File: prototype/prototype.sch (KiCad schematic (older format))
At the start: 31 parts, among them P1 CONN_25X2, P2 CONN_25X2, P3 VGACONN, U1 MC68SEC000

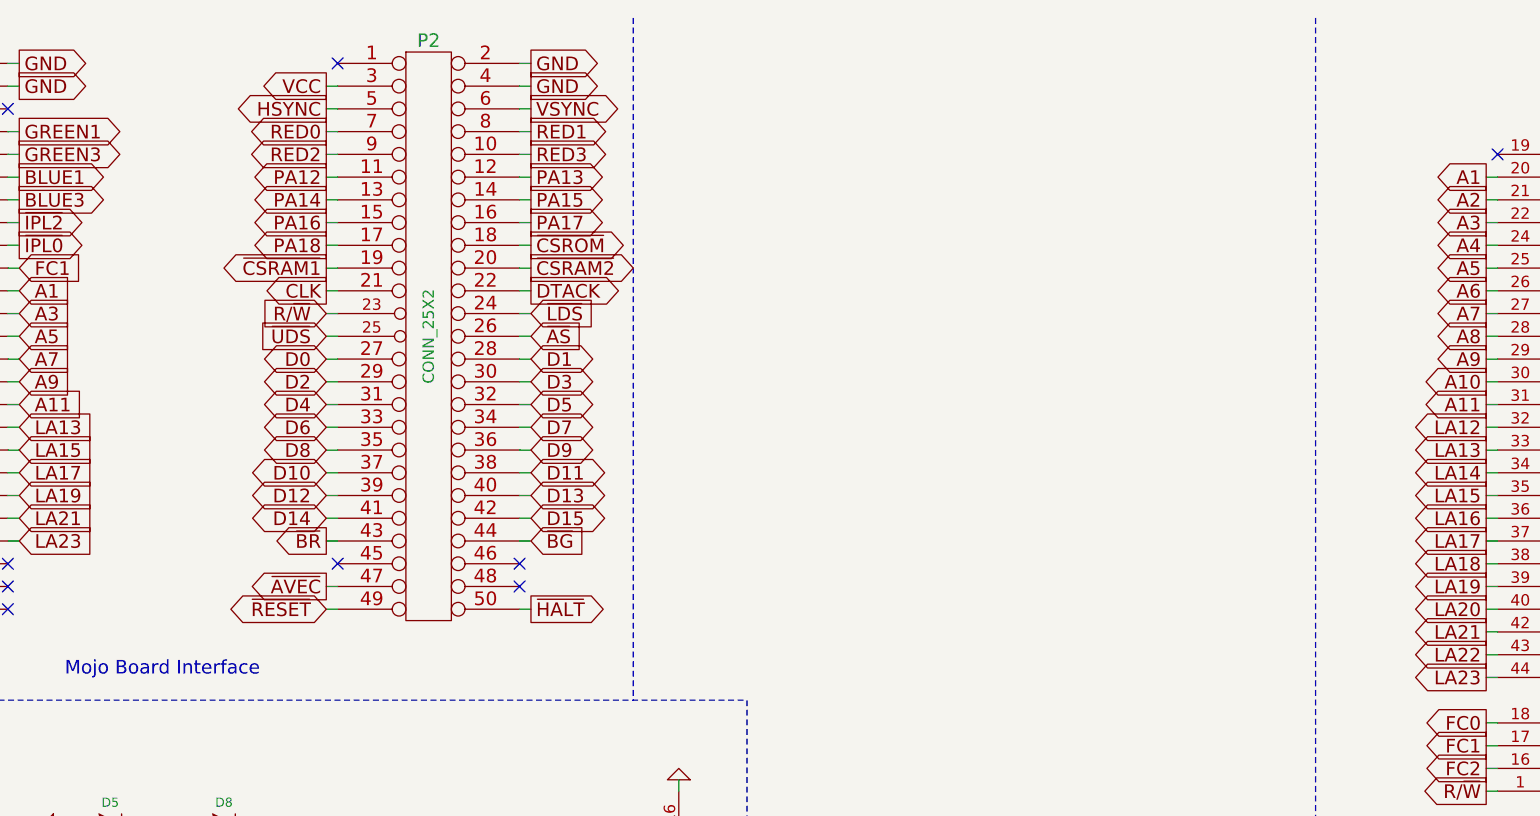
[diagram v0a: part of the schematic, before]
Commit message: Add the flash ROM chip to the prototype schematic.
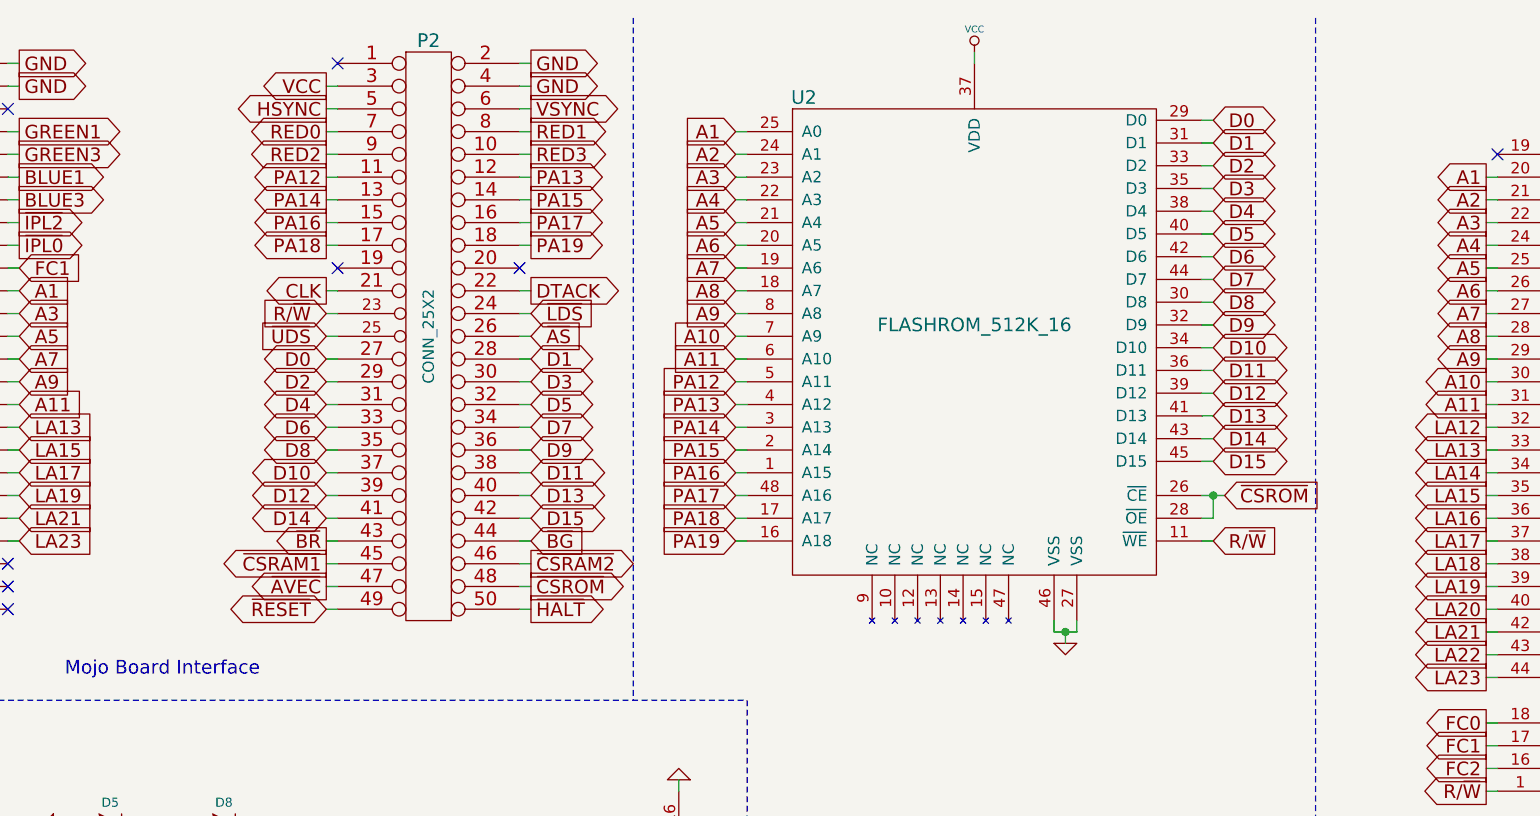
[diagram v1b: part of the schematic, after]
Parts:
- added U2: FLASHROM_512K_16, symbol FLASHROM_512K_16
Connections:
- net A1: now also U2.25 (A0)
- net A10: now also U2.7 (A9)
- net A11: now also U2.6 (A10)
- net A2: now also U2.24 (A1)
- net A3: now also U2.23 (A2)
- net A4: now also U2.22 (A3)
- net A5: now also U2.21 (A4)
- net A6: now also U2.20 (A5)
- net A7: now also U2.19 (A6)
- net A8: now also U2.18 (A7)
- net A9: now also U2.8 (A8)
- net D0: now also U2.29 (D0)
- net D1: now also U2.31 (D1)
- net D10: now also U2.34 (D10)
- net D11: now also U2.36 (D11)
- net D12: now also U2.39 (D12)
- net D13: now also U2.41 (D13)
- net D14: now also U2.43 (D14)
- net D15: now also U2.45 (D15)
- net D2: now also U2.33 (D2)
- net D3: now also U2.35 (D3)
- net D4: now also U2.38 (D4)
- net D5: now also U2.40 (D5)
- net D6: now also U2.42 (D6)
- net D7: now also U2.44 (D7)
- net D8: now also U2.30 (D8)
- net D9: now also U2.32 (D9)
- net GND: now also U2.27 (VSS), U2.46 (VSS)
- net PA12: now also U2.5 (A11)
- net PA13: now also U2.4 (A12)
- net PA14: now also U2.3 (A13)
- net PA15: now also U2.2 (A14)
- net PA16: now also U2.1 (A15)
- net PA17: now also U2.48 (A16)
- net PA18: now also U2.17 (A17)
- net R/~W: now also U2.11 (~WE)
- net VCC: now also U2.37 (VDD)
- net ~CSRAM1: now also P2.45 (P45); no longer P2.19 (P19)
- net ~CSRAM2: now also P2.46 (P46); no longer P2.20 (P20)
- net ~CSROM: now also P2.48 (P48), U2.26 (~CE), U2.28 (~OE); no longer P2.18 (P18)
- new net PA19: P2.18 (P18), U2.16 (A18)
- no-connect marks 19 -> 18

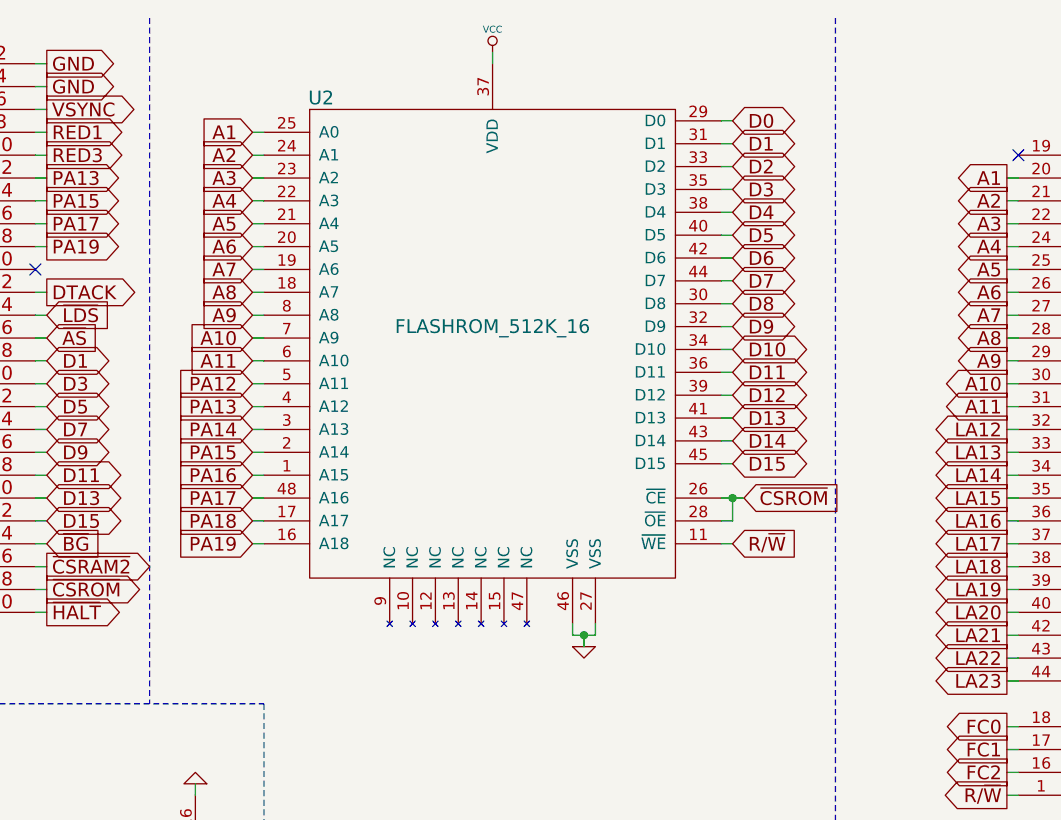
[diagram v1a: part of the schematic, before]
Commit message: Separate schematic sheet for the memory wiring.
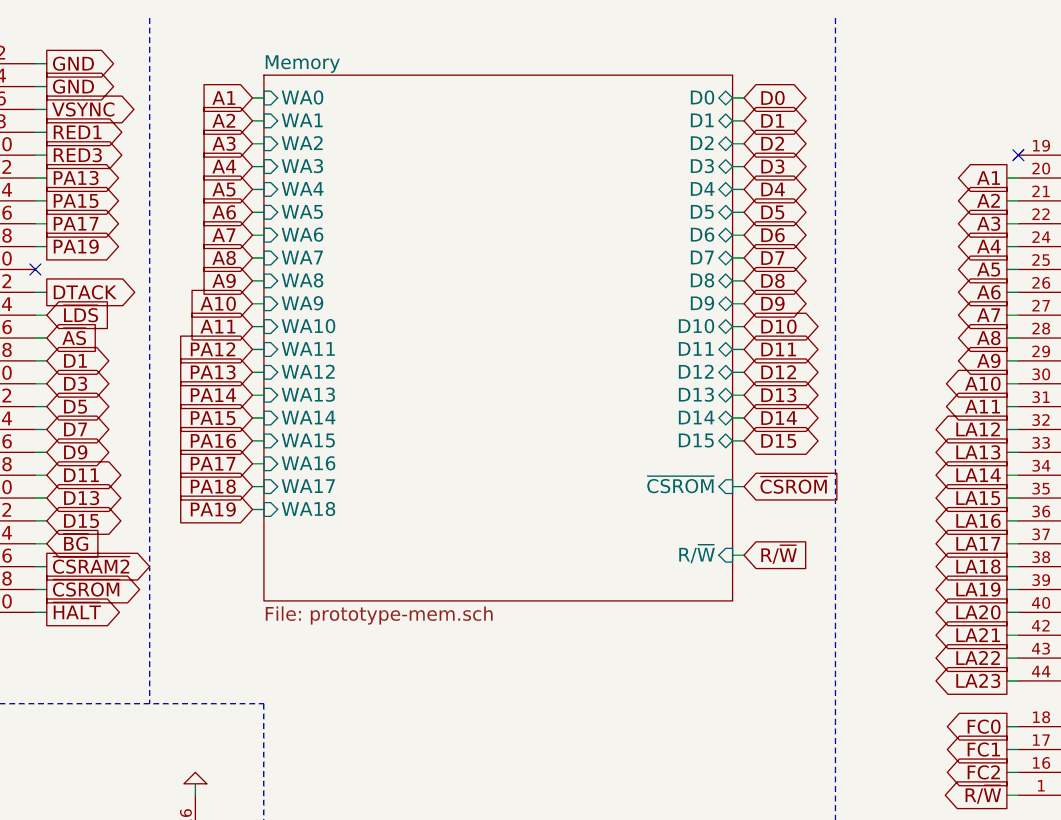
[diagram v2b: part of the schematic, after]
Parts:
- removed U2: FLASHROM_512K_16, symbol FLASHROM_512K_16

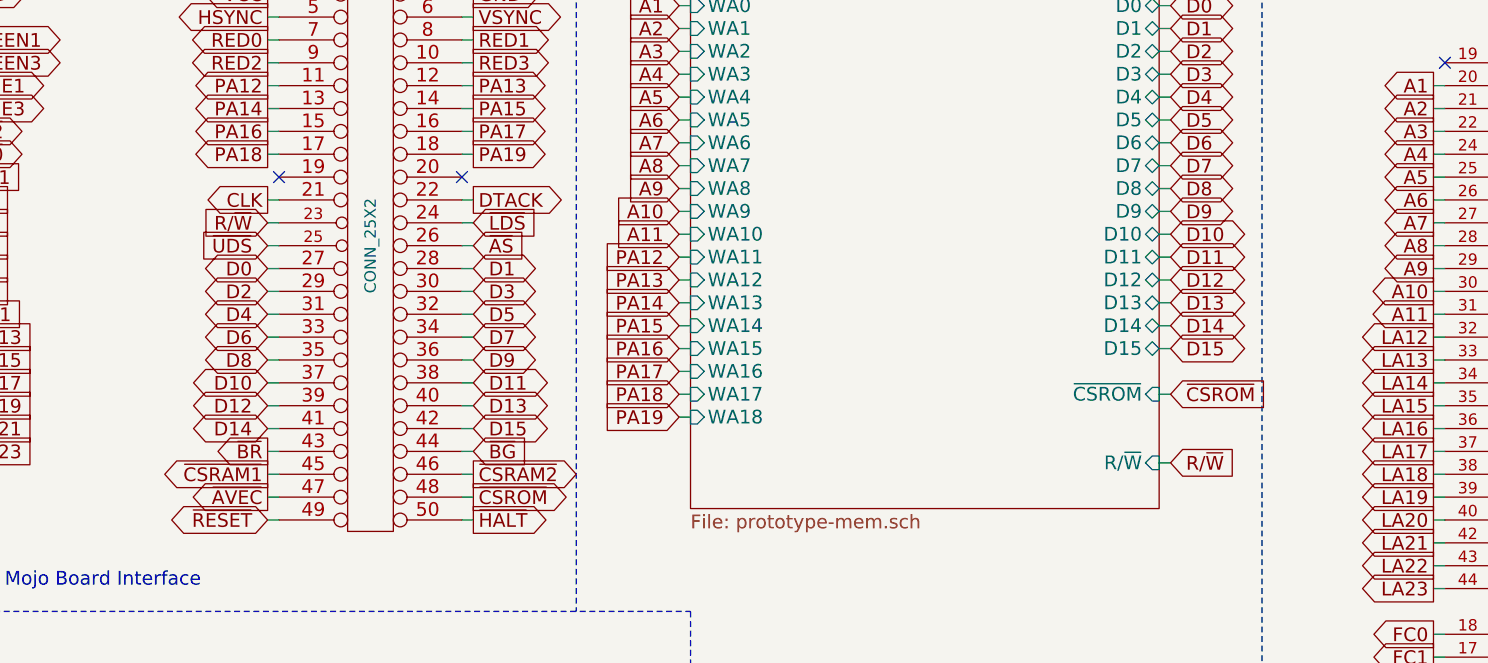
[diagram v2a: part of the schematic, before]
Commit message: Use separate read-enable and write-enable symbols for memory.
Previously we tried to infer these from a combination of the chip select
and R/W signals, but that's not possible without additional glue logic so
we'll just put two more pins on the FPGA output and do the glue logic in
there instead.
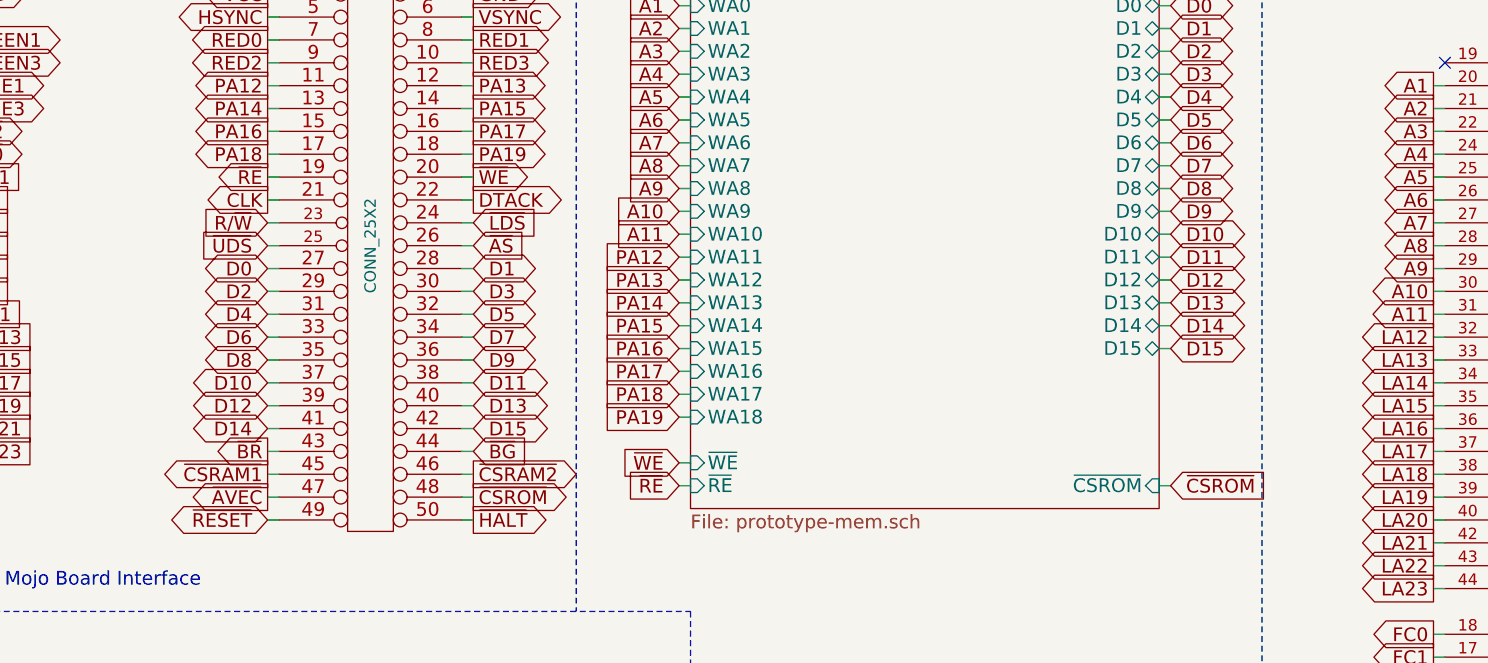
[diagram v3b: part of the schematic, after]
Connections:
- net ~RE: now reaches P2.19 (P19)
- net ~WE: now reaches P2.20 (P20)
- no-connect marks 18 -> 16
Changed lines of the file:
@@
 Wire Wire Line
 	4050 4800 4100 4800
-Text GLabel 7300 2650 2    60   Input ~ 0
+Text GLabel 7300 3050 2    60   Input ~ 0
 ~CSROM
-Text GLabel 7300 2950 2    60   Input ~ 0
-R/~W
 Text GLabel 7300 950  2    60   BiDi ~ 0
 D0
@@
 Wire Wire Line
 	4200 1600 4250 1600
-NoConn ~ 3400 1700
-NoConn ~ 4200 1700
 Text GLabel 5150 950  0    60   Input ~ 0
 A1
@@
 F35 "D14" B R 7250 2350 60
 F36 "D15" B R 7250 2450 60
-F37 "~CSROM" I R 7250 2650 60
-F38 "R/~W" I R 7250 2950 60
+F37 "~CSROM" I R 7250 3050 60
+F38 "~WE" I L 5200 2950 60
+F39 "~RE" I L 5200 3050 60
 $EndSheet
 Wire Wire Line
@@
 Wire Wire Line
 	7250 2450 7300 2450
-Wire Wire Line
-	7250 2650 7300 2650
-Wire Wire Line
-	7250 2950 7300 2950
+Text GLabel 3350 1700 0    60   Output ~ 0
+~RE
+Text GLabel 4250 1700 2    60   Output ~ 0
+~WE
+Wire Wire Line
+	3350 1700 3400 1700
+Wire Wire Line
+	4200 1700 4250 1700
+Text GLabel 5150 3050 0    60   Input ~ 0
+~RE
+Text GLabel 5150 2950 0    60   Input ~ 0
+~WE
+Wire Wire Line
+	5150 2950 5200 2950
+Wire Wire Line
+	5150 3050 5200 3050
+Wire Wire Line
+	7250 3050 7300 3050
 $EndSCHEMATC
